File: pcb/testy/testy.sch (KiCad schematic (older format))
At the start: 13 parts, among them SW0:0 SW_Push, SW0:1 SW_Push, SW0:2 SW_Push, SW1:0 SW_Push, SW1:1 SW_Push, SW1:2 SW_Push, U1 ProMicro

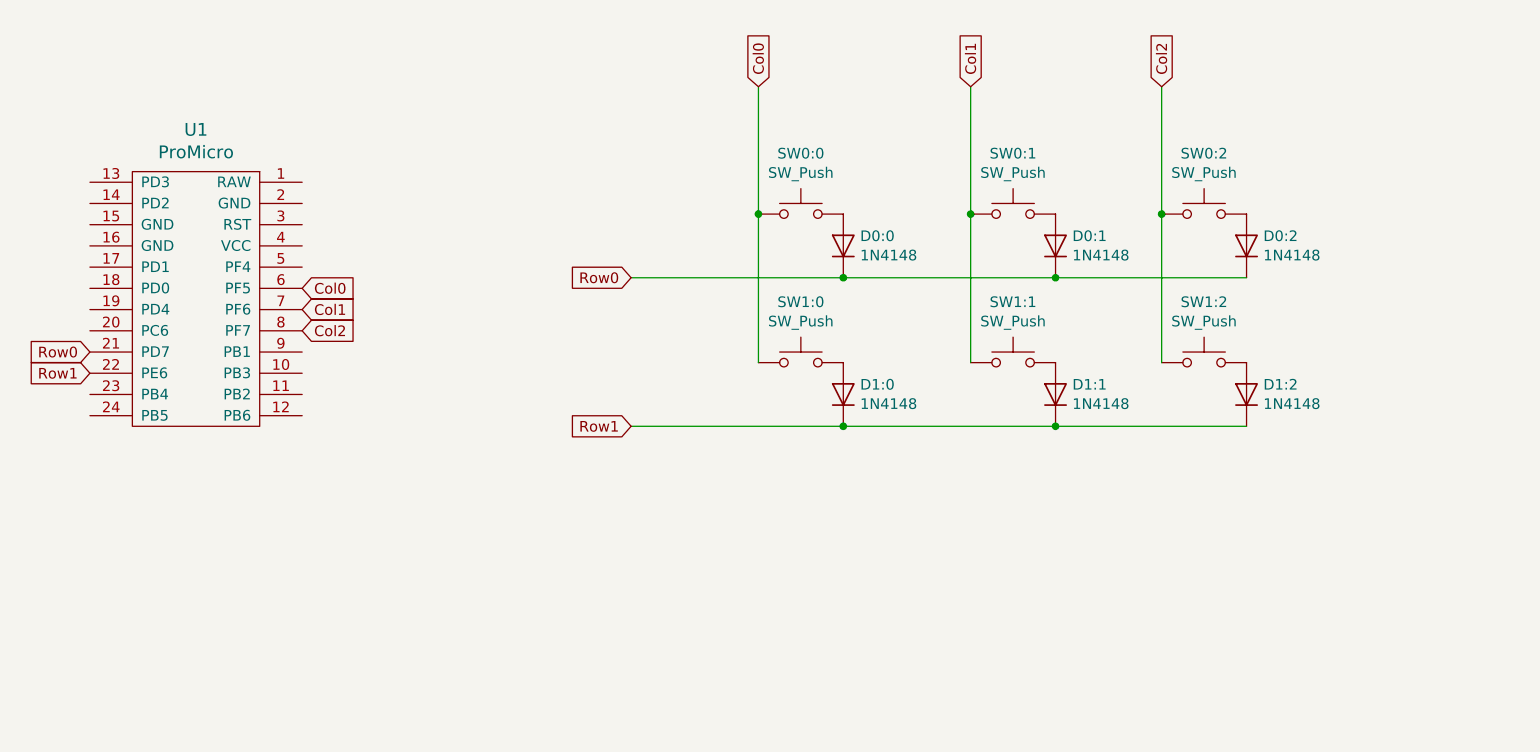
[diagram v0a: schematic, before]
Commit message: chore: enlarged schematic to 4x4, fixed middle layer hole issue. Making a checkpoint before I try to get the netlist to update without destroying all my existing stuff
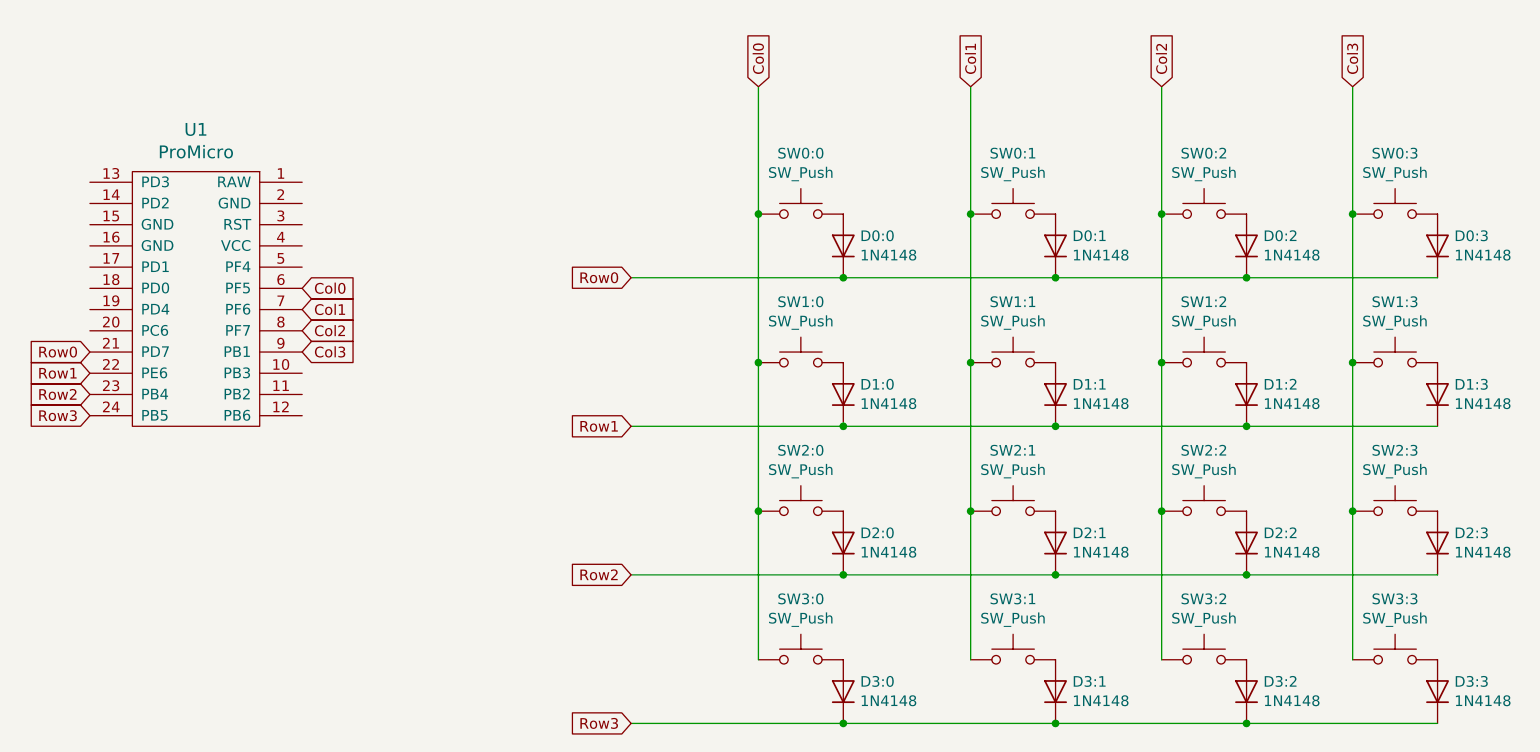
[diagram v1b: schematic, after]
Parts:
- added D0:3, D1:3, D2:0, D2:1, D2:2, D2:3, D3:0, D3:1, D3:2, D3:3: 1N4148, Diode_THT:D_DO-35_SOD27_P7.62mm_Horizontal, symbol Diode:1N4148
- added SW0:3, SW1:3, SW2:0, SW2:1, SW2:2, SW2:3, SW3:0, SW3:1, SW3:2, SW3:3: SW_Push, footprints:Kailh_socket_reversible, symbol Switch:SW_Push
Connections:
- net Col0: now also SW2:0.1, SW3:0.1
- net Col1: now also SW2:1.1, SW3:1.1
- net Col2: now also SW2:2.1, SW3:2.1
- net Row0: now also D0:3.1 (K)
- net Row1: now also D1:3.1 (K)
- net Row2: now reaches U1.23 (PB4)
- net Row2: now also D2:0.1 (K), D2:1.1 (K), D2:2.1 (K), D2:3.1 (K)
- net Row3: now reaches U1.24 (PB5)
- net Row3: now also D3:0.1 (K), D3:1.1 (K), D3:2.1 (K), D3:3.1 (K)
- net Col3: now reaches U1.9 (PB1)
- net Col3: now also SW0:3.1, SW1:3.1, SW2:3.1, SW3:3.1
- new net: D0:3.2 (A), SW0:3.2
- new net: D1:3.2 (A), SW1:3.2
- new net: D2:0.2 (A), SW2:0.2
- new net: D2:1.2 (A), SW2:1.2
- new net: D2:2.2 (A), SW2:2.2
- new net: D3:1.2 (A), SW3:1.2
- new net: D3:2.2 (A), SW3:2.2
- new net: D3:0.2 (A), SW3:0.2
- new net: D2:3.2 (A), SW2:3.2
- new net: D3:3.2 (A), SW3:3.2

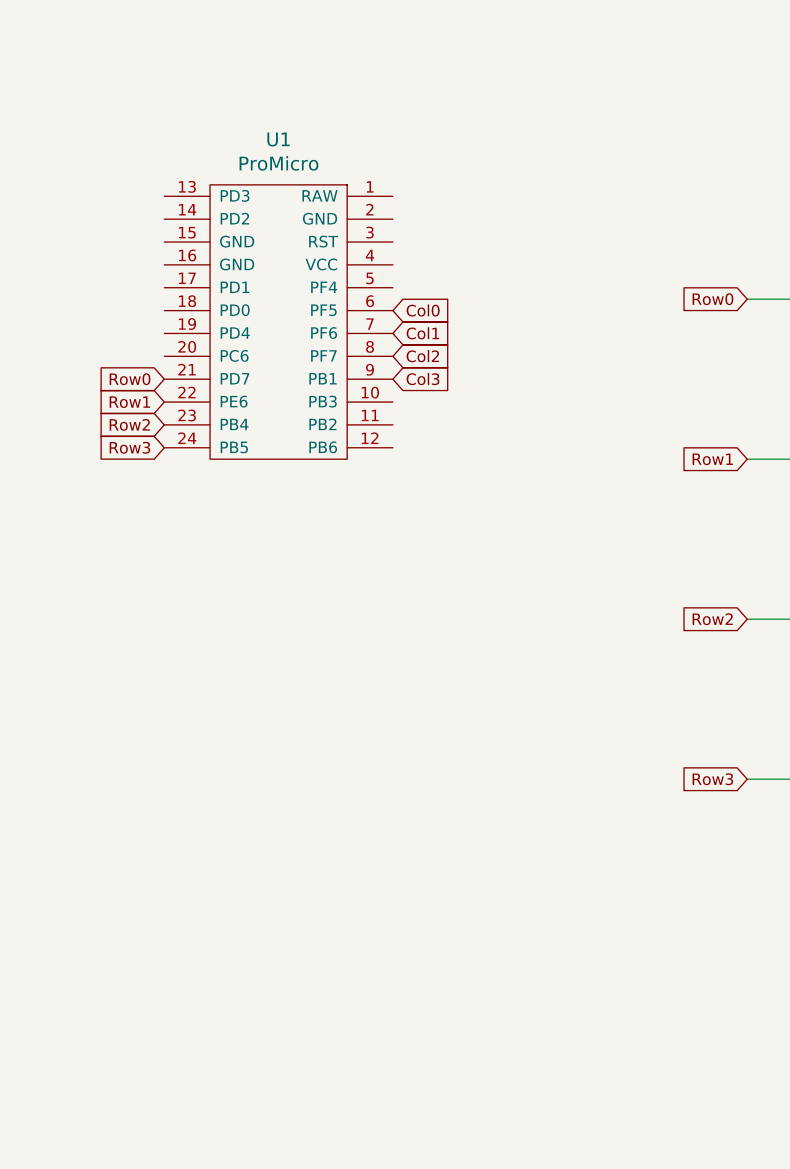
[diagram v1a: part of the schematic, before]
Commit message: feat: add reset switch and TRRS connector, test making promicro snapoff
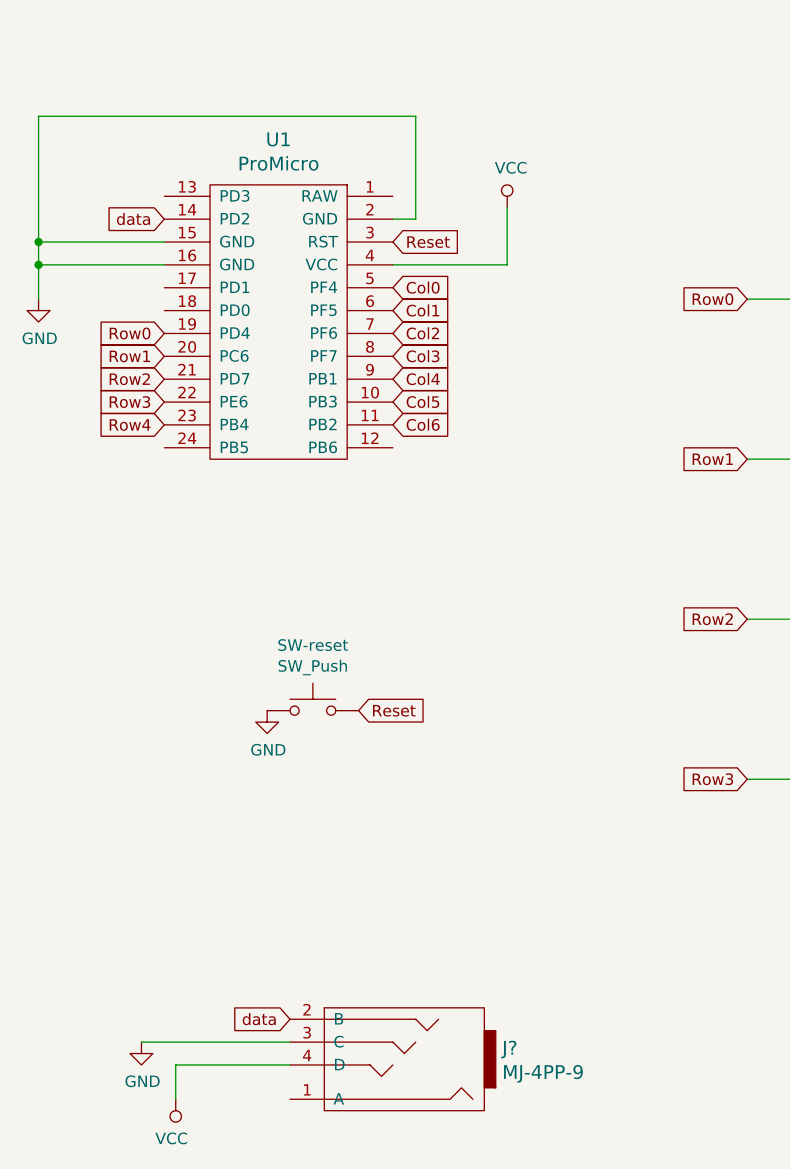
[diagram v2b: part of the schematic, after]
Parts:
- added J?: MJ-4PP-9, symbol mj-4pp-9:MJ-4PP-9
- added SW-reset: SW_Push, footprints:TACT_SWITCH_TVBP06, symbol Switch:SW_Push
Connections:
- net Col0: now also U1.5 (PF4); no longer U1.6 (PF5)
- net Col1: now also U1.6 (PF5); no longer U1.7 (PF6)
- net Col2: now also U1.7 (PF6); no longer U1.8 (PF7)
- net Col3: now also U1.8 (PF7); no longer U1.9 (PB1)
- net Row0: now also U1.19 (PD4); no longer U1.21 (PD7)
- net Row1: now also U1.20 (PC6); no longer U1.22 (PE6)
- net Row2: now also U1.21 (PD7); no longer U1.23 (PB4)
- net Row3: now also U1.22 (PE6); no longer U1.24 (PB5)
- net Col5: now reaches U1.10 (PB3)
- net Col6: now reaches U1.11 (PB2)
- net data: now reaches U1.14 (PD2)
- net data: now also J?.2 (B)
- net GND: now reaches U1.15 (GND)
- net GND: now also U1.16 (GND), U1.2 (GND), J?.3 (C), SW-reset.1
- net Reset: now reaches U1.3 (RST)
- net Reset: now also SW-reset.2
- net VCC: now reaches U1.4 (VCC)
- net VCC: now also J?.4 (D)
- new net Col4: U1.9 (PB1)
- new net Row4: U1.23 (PB4)
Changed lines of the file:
@@
 	0    -1   -1   0
 $EndComp
-Text GLabel 1850 2600 0    50   Input ~ 0
+Text GLabel 1850 2400 0    50   Input ~ 0
 Row0
-Text GLabel 2850 2300 2    50   Input ~ 0
+Text GLabel 2850 2200 2    50   Input ~ 0
 Col0
 Text GLabel 5000 1350 1    50   Input ~ 0
@@
 Wire Wire Line
 	6000 1350 6000 1950
-Text GLabel 2850 2400 2    50   Input ~ 0
+Text GLabel 2850 2300 2    50   Input ~ 0
 Col1
 $Comp
@@
 Text GLabel 4400 2950 0    50   Input ~ 0
 Row1
-Text GLabel 2850 2500 2    50   Input ~ 0
+Text GLabel 2850 2400 2    50   Input ~ 0
 Col2
-Text GLabel 1850 2700 0    50   Input ~ 0
+Text GLabel 1850 2500 0    50   Input ~ 0
 Row1
 $Comp
@@
 Connection ~ 7300 2250
 Connection ~ 7300 2950
-Text GLabel 2850 2600 2    50   Input ~ 0
+Text GLabel 2850 2500 2    50   Input ~ 0
 Col3
-Text GLabel 1850 2800 0    50   Input ~ 0
+Text GLabel 1850 2600 0    50   Input ~ 0
 Row2
 $Comp
@@
 	1    0    0    -1
 $EndComp
-Text GLabel 1850 2900 0    50   Input ~ 0
+Text GLabel 1850 2700 0    50   Input ~ 0
 Row3
 $Comp
@@
 Text GLabel 4400 4350 0    50   Input ~ 0
 Row3
+$Comp
+L mj-4pp-9:MJ-4PP-9 J?
+U 1 1 5DB680F2
+P 2850 5600
+F 0 "J?" H 2372 5527 60  0000 R CNN
+F 1 "MJ-4PP-9" H 2372 5633 60  0000 R CNN
+F 2 "" H 2850 5600 60  0000 C CNN
+F 3 "" H 2850 5600 60  0000 C CNN
+	1    2850 5600
+	-1   0    0    1
+$EndComp
+Text GLabel 1850 1900 0    50   Input ~ 0
+data
+$Comp
+L power:GND #PWR?
+U 1 1 5DB6F1F7
+P 1300 2250
+F 0 "#PWR?" H 1300 2000 50  0001 C CNN
+F 1 "GND" H 1305 2077 50  0000 C CNN
+F 2 "" H 1300 2250 50  0001 C CNN
+F 3 "" H 1300 2250 50  0001 C CNN
+	1    1300 2250
+	1    0    0    -1
+$EndComp
+Wire Wire Line
+	1850 2000 1300 2000
+Wire Wire Line
+	1300 2000 1300 2100
+Wire Wire Line
+	1850 2100 1300 2100
+Connection ~ 1300 2100
+Wire Wire Line
+	1300 2100 1300 2250
+Wire Wire Line
+	2850 1900 2950 1900
+Wire Wire Line
+	2950 1900 2950 1450
+Wire Wire Line
+	2950 1450 1300 1450
+Wire Wire Line
+	1300 1450 1300 2000
+Connection ~ 1300 2000
+Text GLabel 2850 2600 2    50   Input ~ 0
+Col4
+Text GLabel 2850 2700 2    50   Input ~ 0
+Col5
+Text GLabel 2850 2800 2    50   Input ~ 0
+Col6
+Text GLabel 1850 2800 0    50   Input ~ 0
+Row4
+$Comp
+L power:VCC #PWR?
+U 1 1 5DB780CB
+P 3350 1850
+F 0 "#PWR?" H 3350 1700 50  0001 C CNN
+F 1 "VCC" H 3367 2023 50  0000 C CNN
+F 2 "" H 3350 1850 50  0001 C CNN
+F 3 "" H 3350 1850 50  0001 C CNN
+	1    3350 1850
+	1    0    0    -1
+$EndComp
+Wire Wire Line
+	2850 2100 3350 2100
+Wire Wire Line
+	3350 2100 3350 1850
+Text GLabel 2400 5400 0    50   Input ~ 0
+data
+$Comp
+L power:VCC #PWR?
+U 1 1 5DB7BCAC
+P 1900 5750
+F 0 "#PWR?" H 1900 5600 50  0001 C CNN
+F 1 "VCC" H 1918 5923 50  0000 C CNN
+F 2 "" H 1900 5750 50  0001 C CNN
+F 3 "" H 1900 5750 50  0001 C CNN
+	1    1900 5750
+	-1   0    0    1
+$EndComp
+$Comp
+L power:GND #PWR?
+U 1 1 5DB7C36F
+P 1750 5500
+F 0 "#PWR?" H 1750 5250 50  0001 C CNN
+F 1 "GND" H 1755 5327 50  0000 C CNN
+F 2 "" H 1750 5500 50  0001 C CNN
+F 3 "" H 1750 5500 50  0001 C CNN
+	1    1750 5500
+	1    0    0    -1
+$EndComp
+Wire Wire Line
+	1750 5500 2400 5500
+Wire Wire Line
+	2400 5600 1900 5600
+Wire Wire Line
+	1900 5600 1900 5750
+$Comp
+L Switch:SW_Push SW-reset
+U 1 1 5DB80D38
+P 2500 4050
+F 0 "SW-reset" H 2500 4335 50  0000 C CNN
+F 1 "SW_Push" H 2500 4244 50  0000 C CNN
+F 2 "footprints:TACT_SWITCH_TVBP06" H 2500 4250 50  0001 C CNN
+F 3 "~" H 2500 4250 50  0001 C CNN
+	1    2500 4050
+	1    0    0    -1
+$EndComp
+Text GLabel 2850 2000 2    50   Input ~ 0
+Reset
+Text GLabel 2700 4050 2    50   Input ~ 0
+Reset
+$Comp
+L power:GND #PWR?
+U 1 1 5DB88784
+P 2300 4050
+F 0 "#PWR?" H 2300 3800 50  0001 C CNN
+F 1 "GND" H 2305 3877 50  0000 C CNN
+F 2 "" H 2300 4050 50  0001 C CNN
+F 3 "" H 2300 4050 50  0001 C CNN
+	1    2300 4050
+	1    0    0    -1
+$EndComp
 $EndSCHEMATC

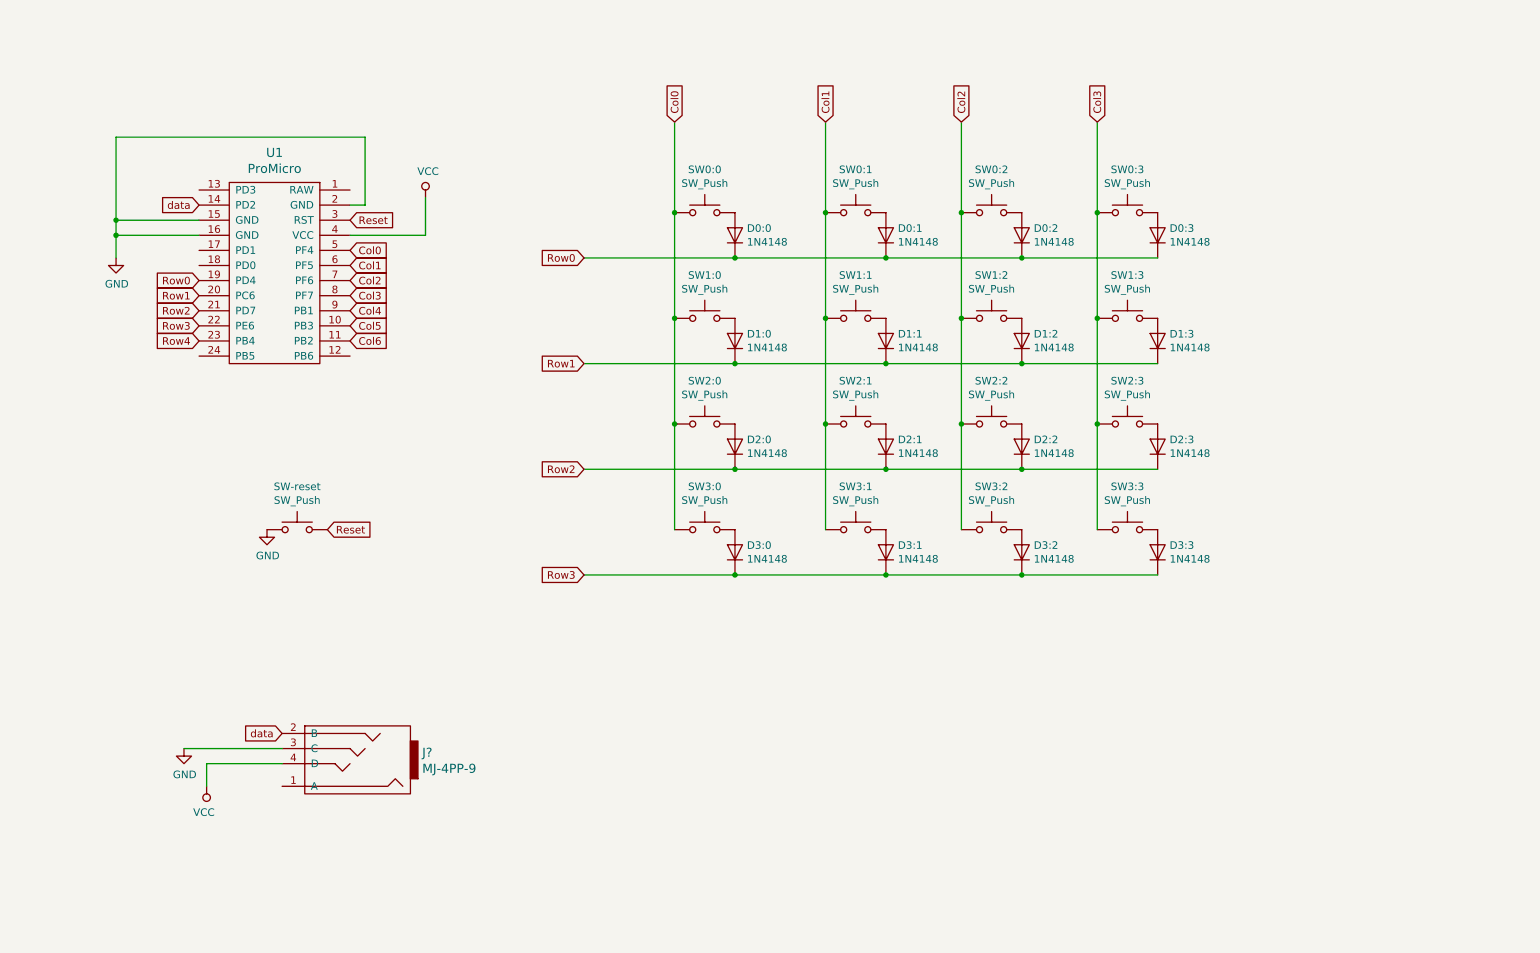
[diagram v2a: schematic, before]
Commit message: feat: add all switches and LEDs to schematic
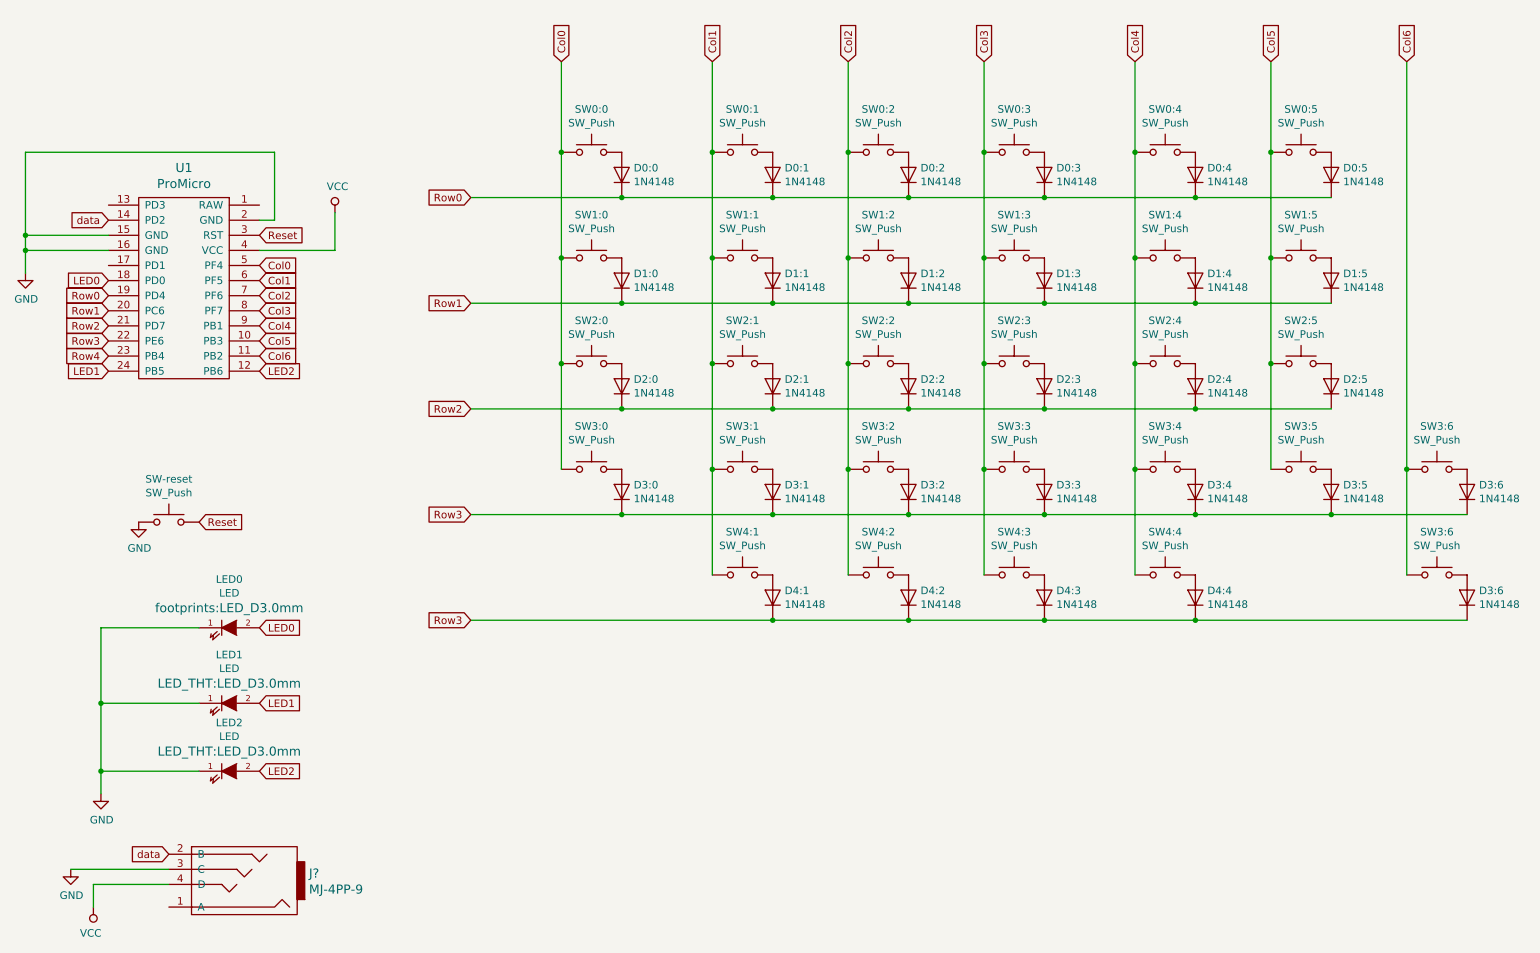
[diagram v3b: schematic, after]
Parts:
- added D0:4, D0:5, D1:4, D1:5, D2:4, D2:5, D3:4, D3:5, D3:6 (x2), D4:1, D4:2, D4:3, D4:4: 1N4148, Diode_THT:D_DO-35_SOD27_P7.62mm_Horizontal, symbol Diode:1N4148
- added LED0: LED, footprints:LED_D3.0mm, symbol led:LED
- added LED1, LED2: LED, LED_THT:LED_D3.0mm, symbol led:LED
- added SW0:4, SW0:5, SW1:4, SW1:5, SW2:4, SW2:5, SW3:4, SW3:5, SW3:6 (x2), SW4:1, SW4:2, SW4:3, SW4:4: SW_Push, footprints:Kailh_socket_reversible, symbol Switch:SW_Push
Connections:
- net Col1: now also SW4:1.1
- net Col2: now also SW4:2.1
- net Col3: now also SW4:3.1
- net Col4: now also SW0:4.1, SW1:4.1, SW2:4.1, SW3:4.1, SW4:4.1
- net Col5: now also SW0:5.1, SW1:5.1, SW2:5.1, SW3:5.1
- net Col6: now also SW3:6.1, SW3:6.1
- net GND: now also LED0.1 (K), LED1.1 (K), LED2.1 (K)
- net Row0: now also D0:4.1 (K), D0:5.1 (K)
- net Row1: now also D1:4.1 (K), D1:5.1 (K)
- net Row2: now also D2:4.1 (K), D2:5.1 (K)
- net Row3: now also D3:4.1 (K), D3:5.1 (K), D3:6.1 (K), D3:6.1 (K), D4:1.1 (K), D4:2.1 (K), D4:3.1 (K), D4:4.1 (K)
- net LED2: now reaches U1.12 (PB6)
- net LED2: now also LED2.2 (A)
- net LED0: now reaches U1.18 (PD0)
- net LED0: now also LED0.2 (A)
- net LED1: now reaches U1.24 (PB5)
- net LED1: now also LED1.2 (A)
- new net: D0:4.2 (A), SW0:4.2
- new net: D0:5.2 (A), SW0:5.2
- new net: D1:4.2 (A), SW1:4.2
- new net: D1:5.2 (A), SW1:5.2
- new net: D2:4.2 (A), SW2:4.2
- new net: D2:5.2 (A), SW2:5.2
- new net: D3:4.2 (A), SW3:4.2
- new net: D3:5.2 (A), SW3:5.2
- new net: D3:6.2 (A), SW3:6.2 (x2)
- new net: D4:1.2 (A), SW4:1.2
- new net: D4:2.2 (A), SW4:2.2
- new net: D4:3.2 (A), SW4:3.2
- new net: D4:4.2 (A), SW4:4.2
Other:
- moved on the sheet: D0:0, D0:1, D0:2, D0:3, D1:0, D1:1, D1:2, D1:3, D2:0, D2:1, D2:2, D2:3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
